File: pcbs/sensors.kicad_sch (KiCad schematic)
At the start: 73 parts, among them U4 CD74HC4067SM, U5 CD74HC4067SM, U6 CD74HC4067SM, U7 CD74HC4067SM, U8 CD74HC4067SM

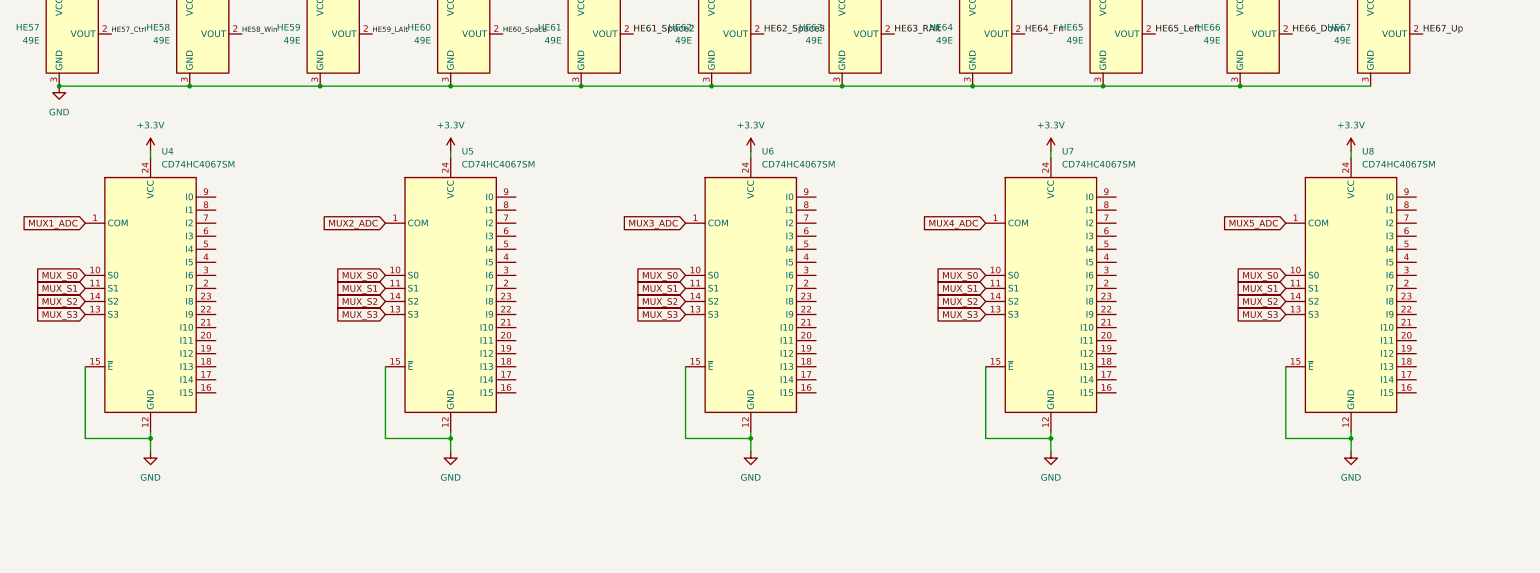
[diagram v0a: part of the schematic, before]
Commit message: new branch for rp2350 version
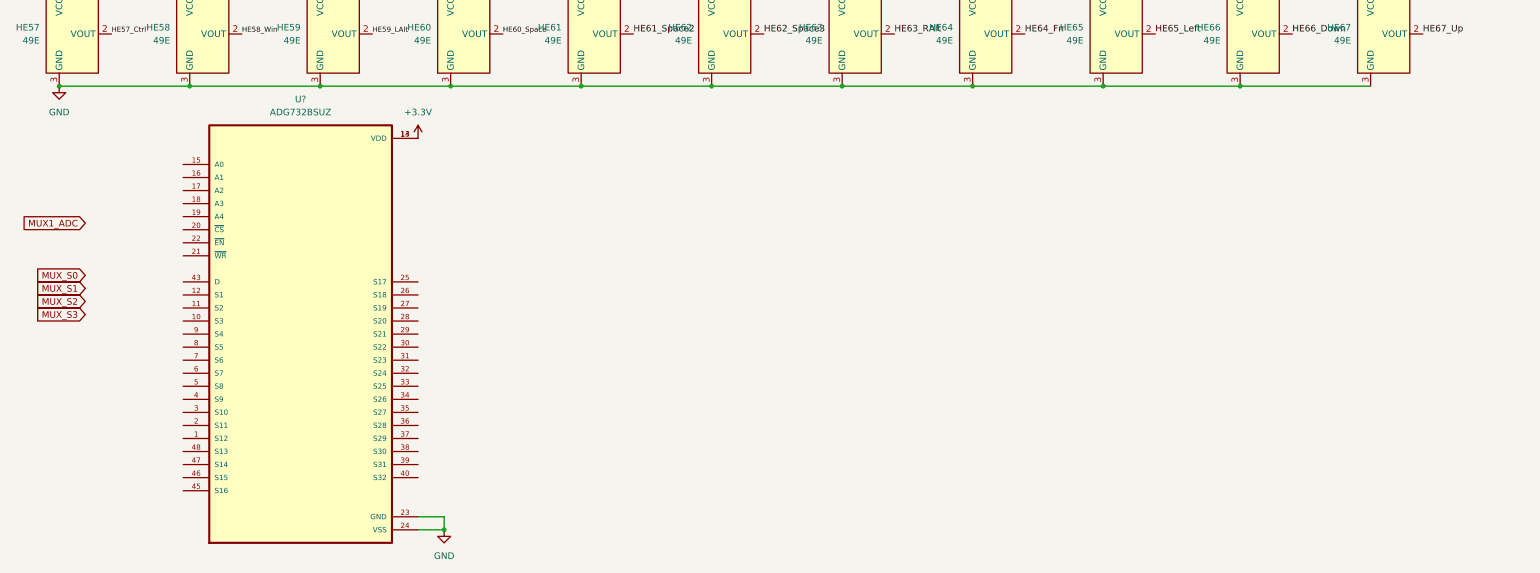
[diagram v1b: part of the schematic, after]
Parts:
- removed U4, U5, U6, U7, U8: CD74HC4067SM, Package_SO:SSOP-24_5.3x8.2mm_P0.65mm, symbol 74xx:CD74HC4067SM
- added U?: ADG732BSUZ, Package_SO:SSOP-24_5.3x8.2mm_P0.65mm, symbol ADG732BSUZ:ADG732BSUZ
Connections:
- net +3.3V: now also U?.13 (VDD), U?.14 (VDD)
- net GND: now also U?.23 (GND), U?.24 (VSS)
